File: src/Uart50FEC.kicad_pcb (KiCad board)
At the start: 2 copper layers, 24 x 27.9 mm, 22 parts, among them J1 105444-0001, J2 B4B-XH-A, Q1 DMP3099L-13, U1 FT232RL, U2 MIC2005A-1

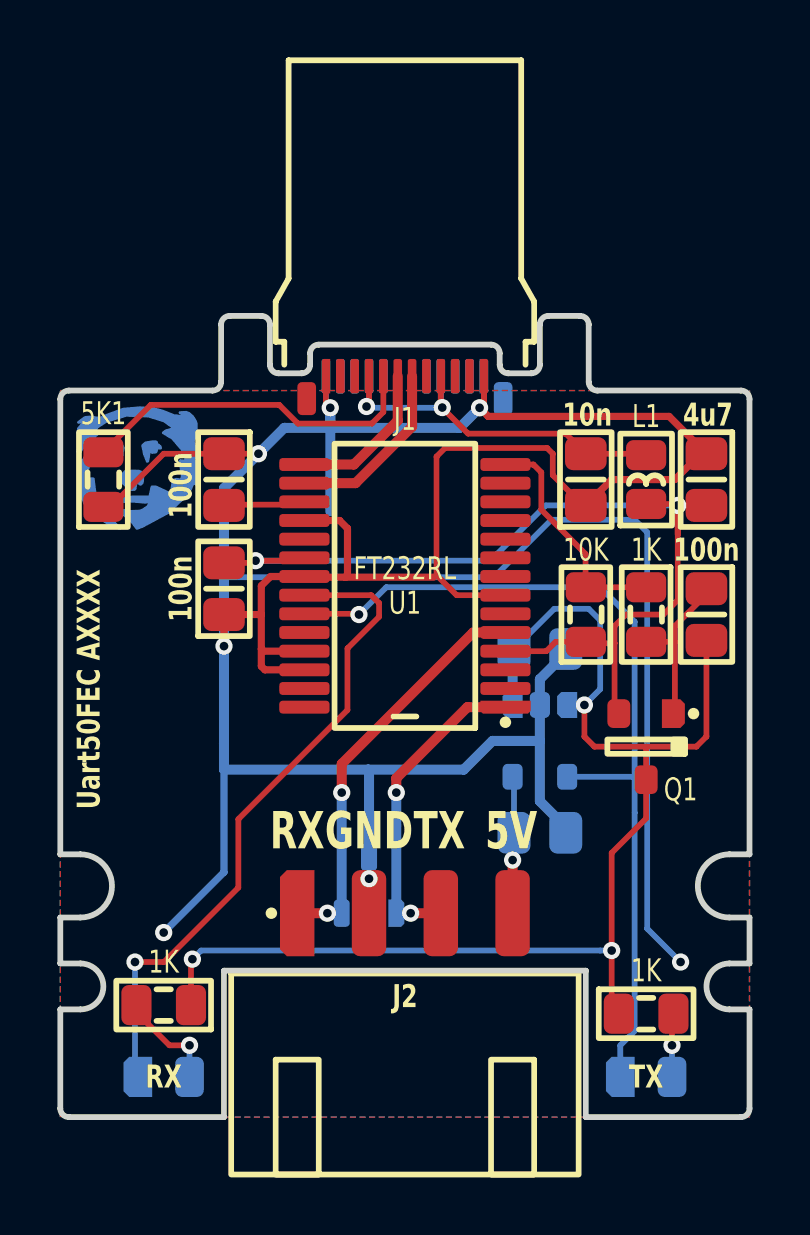
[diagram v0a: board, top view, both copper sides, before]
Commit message: Changed pinout
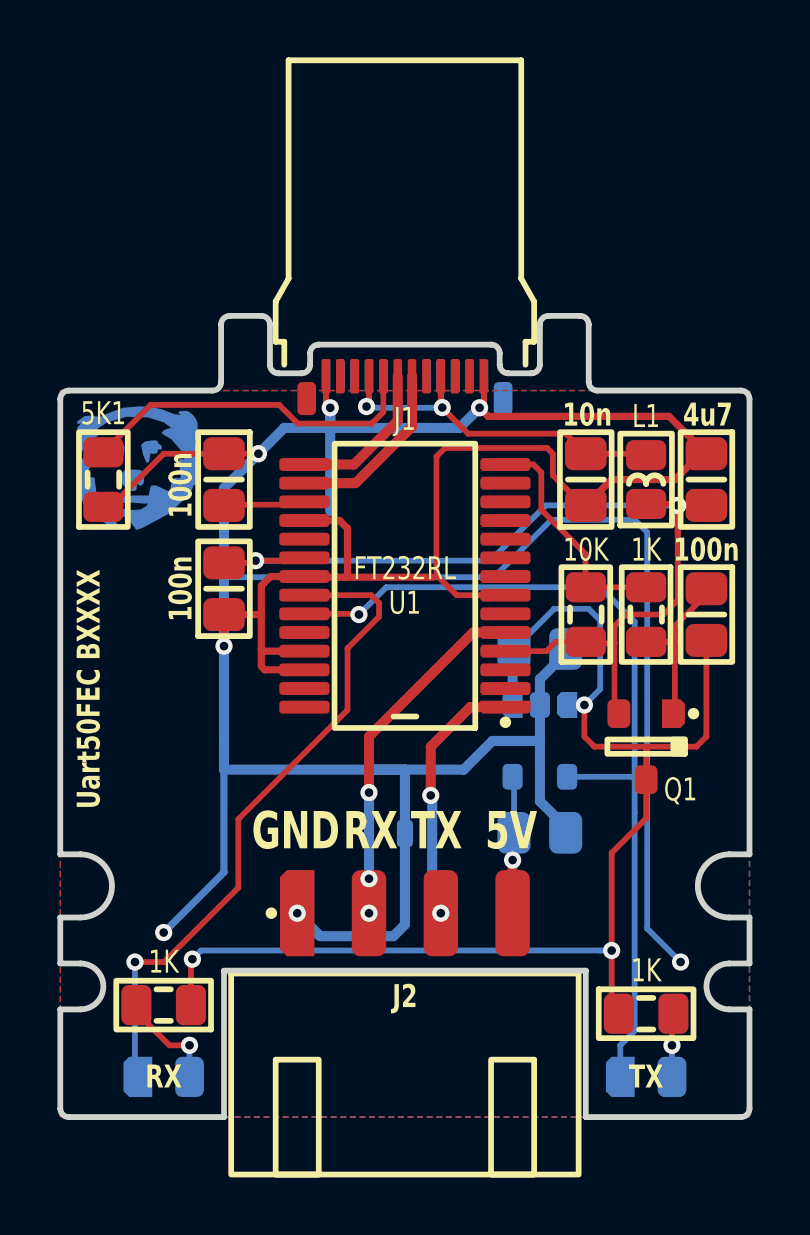
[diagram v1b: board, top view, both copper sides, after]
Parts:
- moved D1 1.50 mm to (32.0, 39.0)
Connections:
- J2 pad 1: RXD -> GND
- J2 pad 2: GND -> RXD
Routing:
- net GND: track 143.7 -> 151.2 mm
- net TXD: track 11.9 -> 9.35 mm
- net RXD: track 15.2 -> 13.6 mm, vias 2 -> 3
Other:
- board text added: "Uart50FEC BXXXX"
- board text removed: "Uart50FEC AXXXX"
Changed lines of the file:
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@@
 			(chamfer_ratio 0.2)
 			(chamfer top_left bottom_left)
-			(net 4 "RXD")
+			(net 7 "GND")
 		)
 		(pad "2" smd roundrect
@@
 			(layers "F.Cu" "F.Paste" "F.Mask")
 			(roundrect_rratio 0.25)
-			(net 7 "GND")
+			(net 4 "RXD")
 		)
 		(pad "3" smd roundrect
@@
 	(footprint "Medo64:D TVS SM05T1G (SOT23-3)"
 		(layer "B.Cu")
-		(at 30.75 39.825 180)
+		(at 32 39 180)
 		(descr "SM05T1G [SM05T1GOSCT-ND]")
 		(property "Reference" "D1"
@@
 	)
 	(gr_text "RX"
-		(at 28.25 38.7 0)
+		(at 30.8 38.7 0)
 		(layer "F.SilkS" knockout)
 		(effects
@@
 	)
 	(gr_text "GND"
-		(at 30.75 38.7 0)
+		(at 28.2 38.7 0)
 		(layer "F.SilkS" knockout)
 		(effects
@@
 	)
 	(gr_text "TX"
-		(at 33.2 38.7 0)
+		(at 33.1 38.7 0)
 		(layer "F.SilkS" knockout)
 		(effects
@@
 		)
 	)
-	(gr_text "Uart50FEC AXXXX"
+	(gr_text "Uart50FEC BXXXX"
 		(at 21 33 90)
 		(layer "F.SilkS")
@@
 	(segment
 		(start 33.05 39.7)
-		(end 33.05 40.8)
+		(end 33.05 40.59997)
 		(width 0.35)
 		(layer "F.Cu")
@@
 	)
 	(segment
-		(start 35.5 33.625)
-		(end 34.175 33.625)
+		(start 32.9 35)
+		(end 32.9 36.7)
 		(width 0.35)
 		(layer "F.Cu")
@@
 	)
 	(segment
-		(start 34.175 33.625)
-		(end 31.7 36.1)
+		(start 35.5 33.625)
+		(end 34.275 33.625)
 		(width 0.35)
 		(layer "F.Cu")
@@
 	)
 	(segment
-		(start 31.7 36.1)
-		(end 31.7 36.6)
+		(start 34.275 33.625)
+		(end 32.9 35)
 		(width 0.35)
 		(layer "F.Cu")
@@
 	)
 	(segment
-		(start 33.05 40.8)
-		(end 32.200004 40.8)
+		(start 33.05 40.59997)
+		(end 33.25003 40.8)
 		(width 0.35)
 		(layer "F.Cu")
@@
 	)
 	(via
-		(at 32.200004 40.8)
+		(at 33.25003 40.8)
 		(size 0.6)
 		(drill 0.3)
@@
 	)
 	(via
-		(at 31.7 36.6)
+		(at 32.9 36.7)
 		(size 0.6)
 		(drill 0.3)
@@
 	)
 	(segment
-		(start 31.7 37.775)
-		(end 31.7 40.8)
-		(width 0.35)
-		(layer "B.Cu")
-		(net 2)
-	)
-	(segment
-		(start 31.7 40.8)
-		(end 32.200004 40.8)
+		(start 32.95 36.75)
+		(end 32.9 36.7)
 		(width 0.35)
 		(layer "B.Cu")
@@
 	)
 	(segment
-		(start 31.7 36.6)
-		(end 31.7 37.725)
+		(start 32.95 39.975)
+		(end 32.95 36.75)
 		(width 0.35)
 		(layer "B.Cu")
@@
 	)
 	(segment
-		(start 34.375 31.025)
-		(end 29.8 35.6)
+		(start 35.5 31.025)
+		(end 34.375 31.025)
 		(width 0.35)
 		(layer "F.Cu")
@@
 	)
 	(segment
-		(start 28.25 40.799994)
-		(end 29.3 40.799994)
+		(start 30.75 40.8)
+		(end 30.75 39.6)
 		(width 0.35)
 		(layer "F.Cu")
@@
 	)
 	(segment
-		(start 29.8 35.6)
-		(end 29.8 36.6)
+		(start 34.375 31.025)
+		(end 30.75004 34.64996)
 		(width 0.35)
 		(layer "F.Cu")
@@
 	)
 	(segment
-		(start 35.5 31.025)
-		(end 34.375 31.025)
+		(start 30.75004 34.64996)
+		(end 30.75004 36.6)
 		(width 0.35)
 		(layer "F.Cu")
 		(net 4)
 	)
-	(segment
-		(start 28.25 39.95)
-		(end 28.25 40.799994)
-		(width 0.35)
-		(layer "F.Cu")
+	(via
+		(at 30.75 39.6)
+		(size 0.6)
+		(drill 0.3)
+		(layers "F.Cu" "B.Cu")
 		(net 4)
 	)
 	(via
-		(at 29.8 36.6)
+		(at 30.75004 36.6)
 		(size 0.6)
 		(drill 0.3)
@@
 	)
 	(via
-		(at 29.3 40.799994)
+		(at 30.75002 40.79999)
 		(size 0.6)
 		(drill 0.3)
@@
 	)
 	(segment
-		(start 29.8 40.799994)
-		(end 29.3 40.799994)
+		(start 30.75002 36.60002)
+		(end 30.75004 36.6)
 		(width 0.35)
 		(layer "B.Cu")
@@
 	)
 	(segment
-		(start 29.8 36.6)
-		(end 29.8 40.799994)
+		(start 30.75002 40.79999)
+		(end 30.75002 36.60002)
 		(width 0.35)
 		(layer "B.Cu")
@@
 	)
 	(segment
-		(start 30.75 40.8)
-		(end 30.75 39.6)
-		(width 0.35)
-		(layer "F.Cu")
-		(net 7)
-	)
-	(segment
 		(start 29.925 29.1)
 		(end 33 29.1)
@@
 	)
 	(segment
+		(start 28.25 39.95)
+		(end 28.25 40.799994)
+		(width 0.35)
+		(layer "F.Cu")
+		(net 7)
+	)
+	(segment
 		(start 28.5 32.325)
 		(end 27.125 32.325)
@@
 	)
 	(via
-		(at 30.75 39.6)
+		(at 29.4 23.2)
 		(size 0.6)
 		(drill 0.3)
@@
 	)
 	(via
-		(at 29.4 23.2)
+		(at 34.6 23.2)
 		(size 0.6)
 		(drill 0.3)
@@
 	)
 	(via
-		(at 34.6 23.2)
+		(at 23.6 41.474017)
 		(size 0.6)
 		(drill 0.3)
@@
 	)
 	(via
-		(at 23.6 41.474017)
+		(at 28.249996 40.8)
 		(size 0.6)
 		(drill 0.3)
@@
 	)
 	(segment
-		(start 30.75 35.825)
-		(end 30.75 38.85)
+		(start 30.725 35.8)
+		(end 32 35.8)
 		(width 0.35)
 		(layer "B.Cu")
@@
 	)
 	(segment
-		(start 33.9 23.9)
-		(end 34.6 23.2)
+		(start 32 41.2)
+		(end 31.6 41.6)
 		(width 0.35)
 		(layer "B.Cu")
@@
 	)
 	(segment
-		(start 29.4 23.9)
-		(end 27.8 23.9)
+		(start 32 38.025)
+		(end 32 41.2)
 		(width 0.35)
 		(layer "B.Cu")
@@
 	)
 	(segment
-		(start 30.725 35.8)
-		(end 30.75 35.825)
+		(start 31.6 41.6)
+		(end 29.049996 41.6)
+		(width 0.35)
+		(layer "B.Cu")
+		(net 7)
+	)
+	(segment
+		(start 33.9 23.9)
+		(end 34.6 23.2)
+		(width 0.35)
+		(layer "B.Cu")
+		(net 7)
+	)
+	(segment
+		(start 29.4 23.9)
+		(end 27.8 23.9)
 		(width 0.35)
 		(layer "B.Cu")
@@
 	)
 	(segment
+		(start 29.049996 41.6)
+		(end 28.249996 40.8)
+		(width 0.35)
+		(layer "B.Cu")
+		(net 7)
+	)
+	(segment
 		(start 36.7 32.65)
 		(end 37.6 31.75)
@@
 	)
 	(segment
+		(start 32 35.8)
+		(end 32 38.025)
+		(width 0.35)
+		(layer "B.Cu")
+		(net 7)
+	)
+	(segment
 		(start 40.436628 41.336628)
 		(end 40.436628 27.536628)
@@
 		(min_thickness 0.3)
 		(filled_areas_thickness no)
-		(fill yes
+		(fill
 			(thermal_gap 0.5)
 			(thermal_bridge_width 0.5)

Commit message: More output capacitance
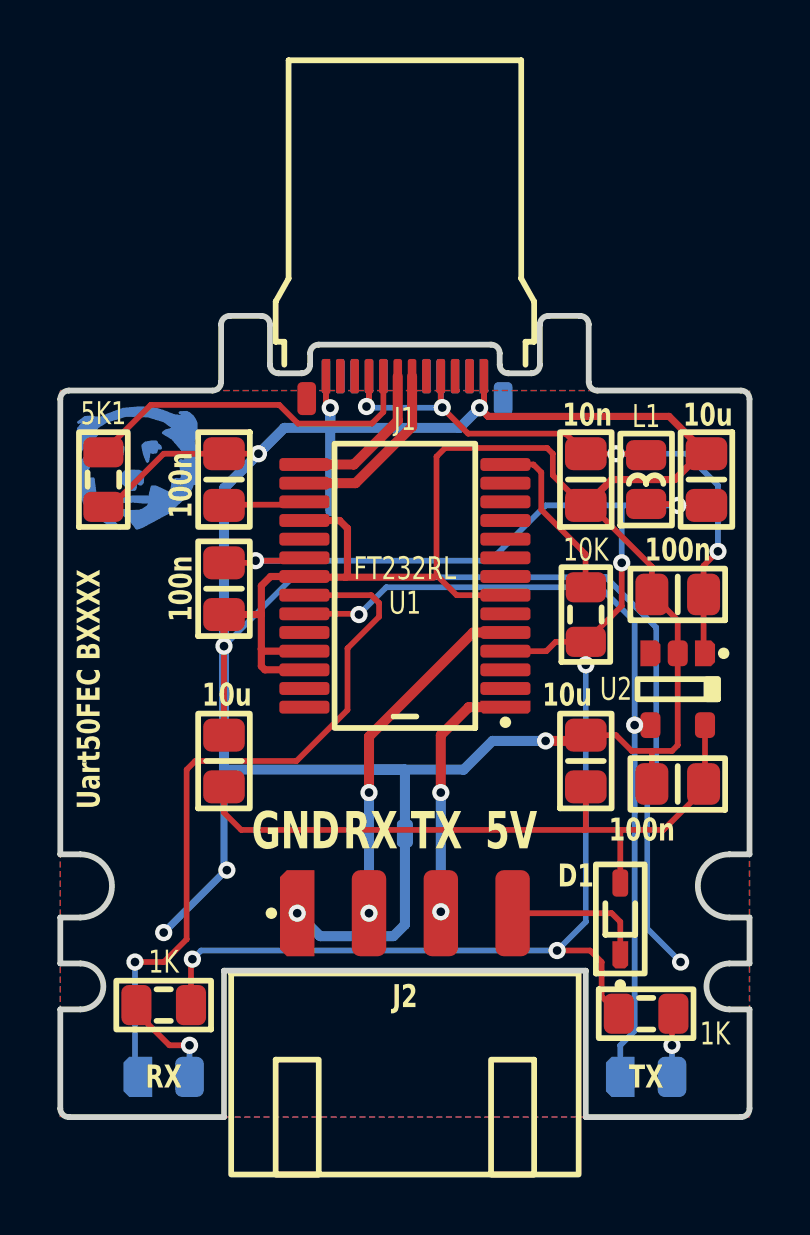
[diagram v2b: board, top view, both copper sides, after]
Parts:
- removed the C4 at (42.5, 30.4)
- removed Q1: DMP3099L-13, Medo64:Q MOSFET-P (SOT23-3)
- removed the R3 at (40.4, 30.4)
- added C7: 10u, Medo64:C (0805), F.Cu at (38.3, 35.5)
- added C8: 10u, Medo64:C (0805), F.Cu at (25.7, 35.5)
- added D1: CUS08F30, Medo64:D (SOD323), F.Cu at (39.5, 41.0)
- C4: renamed from C5; value 1uF -> 100n; moved to F.Cu
- C5: renamed from C7; value 10uF -> 100n; moved to F.Cu
- C6: value 4u7 -> 10u
- D2: renamed from D1; footprint Medo64:D TVS SM05T1G (SOT23-3) -> Medo64:D TVS 5V [SM05T1G] (SOT23-3)
- U2: footprint Medo64:U LoadSwitch 500mA [MIC2005A-1] (SOT23-5) -> Medo64:U LoadSwitch 500mA [MIC2005A-2] (SOT23-5); moved to F.Cu
- moved C4 5.16 mm to (41.5, 29.7), turned to 180 degrees
- moved U2 5.13 mm to (41.5, 33.0)
- moved C5 5.09 mm to (41.5, 36.3), turned to 180 degrees
- renumbered R4 to R3, R5 to R4
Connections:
- C1 pad 2: USB_Vin -> USB_5V
- C4 pad 1: 5V_SW -> USB_5V
- C5 pad 1: Vout -> OUT_5V
- J1 pad A4: USB_Vin -> USB_5V
- J1 pad A9: USB_Vin -> USB_5V
- J1 pad B04: USB_Vin -> USB_5V
- J1 pad B09: USB_Vin -> USB_5V
- J2 pad 4: Vout -> OUT_V+
- L1 pad 2: USB_Vin -> USB_5V
- R1 pad 1: 5V_SW -> 5V
- R2 pad 1: 5V_SW -> 5V
- U2 pad 1: 5V_SW -> USB_5V
- U2 pad 5: Vout -> OUT_5V
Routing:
- net 5V_SW: track 43.8 -> 0.00 mm, vias 3 -> 0
- net USB_5V: track 0.00 -> 24.7 mm, vias 0 -> 4
- net OUT_5V: track 0.00 -> 23.8 mm
- net 5V: track 34.1 -> 57.7 mm, vias 2 -> 6
- net USB_Vin: track 14.7 -> 0.00 mm, vias 2 -> 0
- net GND: track 151.2 -> 157.9 mm, vias 7 -> 9
- net PWREN#': track 5.56 -> 0.00 mm
- net OUT_V+: track 0.00 -> 5.02 mm
- net Vout: track 4.65 -> 0.00 mm, vias 1 -> 0
- net PWREN#: track 8.11 -> 6.00 mm
- net LED_RX#: track 23.2 -> 25.3 mm
- net LED_TX#: track 30.8 -> 29.0 mm, vias 1 -> 2
- net RXD: track 13.6 -> 12.4 mm, vias 3 -> 2

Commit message: Swapped load switch
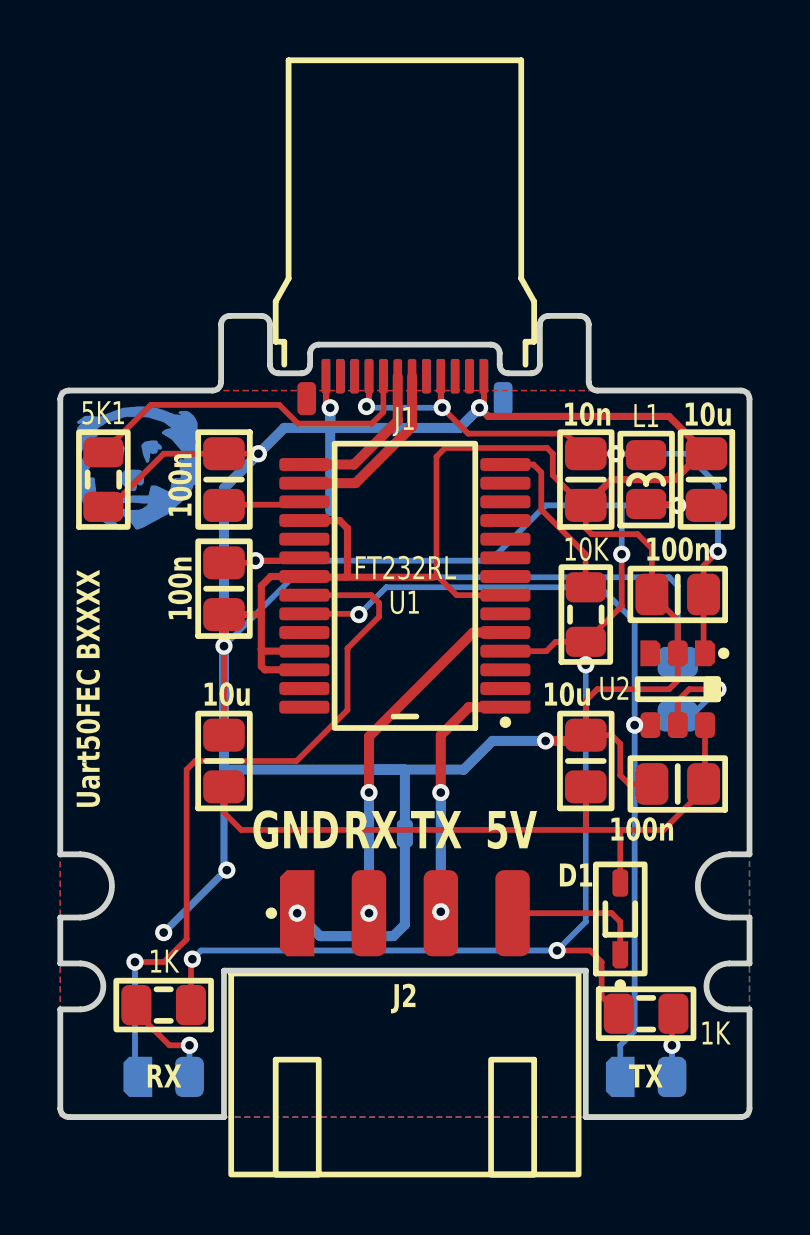
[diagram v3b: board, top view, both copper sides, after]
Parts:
- added R5: 68K, Medo64:R (0805), B.Cu at (41.5, 33.0)
- U2: footprint Medo64:U LoadSwitch 500mA [MIC2005A-2] (SOT23-5) -> Medo64:U LoadSwitch Adjustable [AP22652W6-7] (SOT23-6)
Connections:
- U2 pad 5: OUT_5V -> ILIM
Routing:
- net GND: track 157.9 -> 150.7 mm, vias 9 -> 8
- net ILIM: track 0.00 -> 3.76 mm, vias 0 -> 1
